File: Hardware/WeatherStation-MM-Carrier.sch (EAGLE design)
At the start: 88 parts, among them J11 microSD, J13 RJ11 - WIND, J15 MICROMOD-2222-C, J2 JTAG, J3 QWIIC_RIGHT_ANGLE, J7 RJ11 - RAIN, U1 BME280, U2 VEML6075, U3 AS3935, U5 AP7361C-33FGE

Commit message: Implementing some changes from design check list
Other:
- note added: "Range: 4.2 - 5.2V"
- moved on the sheet: C6, C7, C8, J4, L1, R19, R6, U3

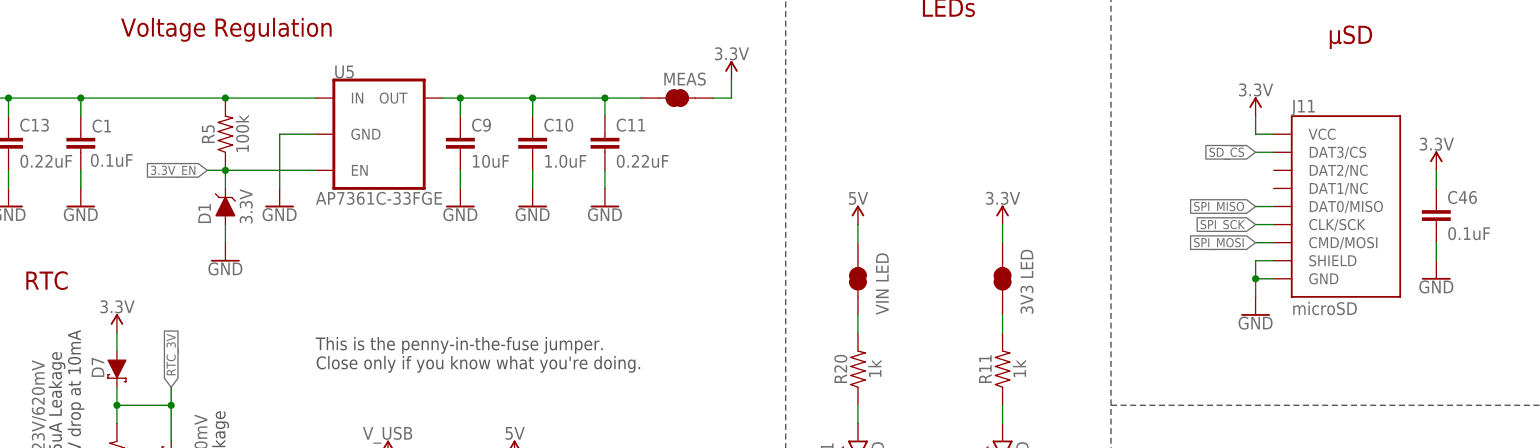
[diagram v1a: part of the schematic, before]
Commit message: Added jumper on 3.3V_EN
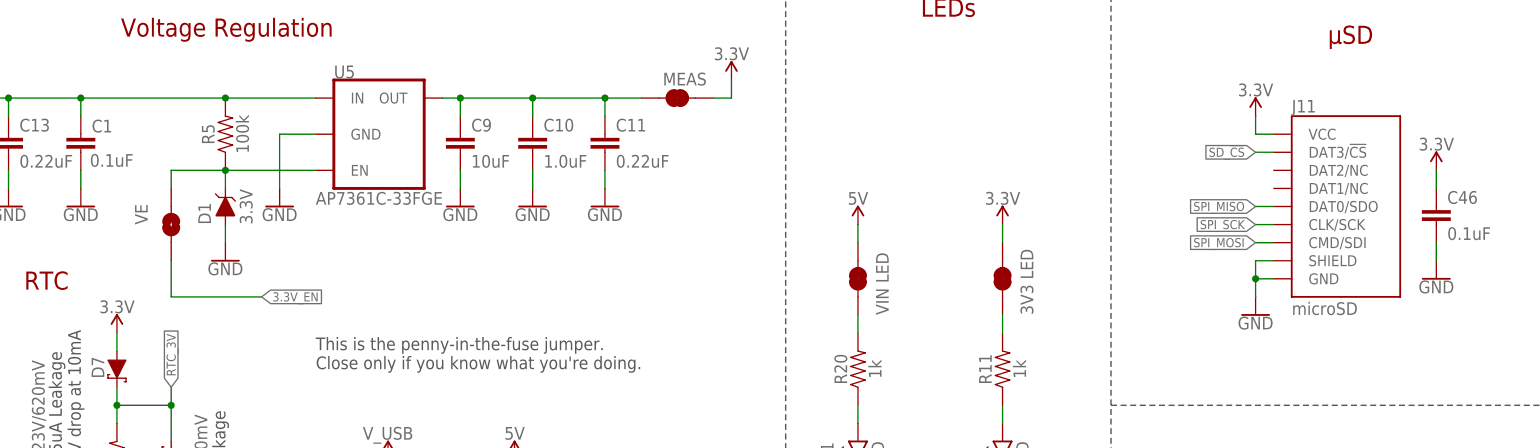
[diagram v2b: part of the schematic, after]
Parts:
- added JP6: VE, SparkFun-Jumpers:JUMPER-SMT_2_NO_SILK
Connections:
- net 3.3V_EN: now also JP6.1, JP6.2
- net SD_!CS!: now also J11.DAT3/!CS!; no longer J11.DAT3/CS
- net SPI_MISO: now also J11.DAT0/SDO; no longer J11.DAT0/MISO
- net SPI_MOSI: now also J11.CMD/SDI; no longer J11.CMD/MOSI
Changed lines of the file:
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@@
 <part name="JP3" library="SparkFun-Jumpers" deviceset="JUMPER-SMT_2_NC_TRACE" device="_SILK" package3d_urn="urn:adsk.eagle:package:39281/1" value="UV"/>
 <part name="JP5" library="SparkFun-Jumpers" deviceset="JUMPER-SMT_3_2-NC_TRACE" device="_SILK" package3d_urn="urn:adsk.eagle:package:39289/1" value="VIN/3"/>
+<part name="JP6" library="SparkFun-Jumpers" deviceset="JUMPER-SMT_2_NO" device="_SILK" package3d_urn="urn:adsk.eagle:package:39279/1" value="VE"/>
 </parts>
 <sheets>
@@
 <attribute name="VALUE" x="136.779" y="30.48" size="1.778" layer="96" font="vector" rot="R270" align="top-left"/>
 </instance>
+<instance part="JP6" gate="G$1" x="35.56" y="241.3" smashed="yes" rot="R90">
+<attribute name="VALUE" x="30.48" y="241.3" size="1.778" layer="96" font="vector" rot="R90" align="top-left"/>
+</instance>
 </instances>
 <busses>
@@
 <wire x1="190.5" y1="238.76" x2="187.96" y2="238.76" width="0.1524" layer="91"/>
 <label x="187.96" y="238.76" size="1.27" layer="95" rot="R180" xref="yes"/>
-<pinref part="J11" gate="G$1" pin="CMD/MOSI"/>
+<pinref part="J11" gate="G$1" pin="CMD/SDI"/>
 </segment>
 <segment>
@@
 <wire x1="190.5" y1="243.84" x2="187.96" y2="243.84" width="0.1524" layer="91"/>
 <label x="187.96" y="243.84" size="1.27" layer="95" rot="R180" xref="yes"/>
-<pinref part="J11" gate="G$1" pin="DAT0/MISO"/>
+<pinref part="J11" gate="G$1" pin="DAT0/SDO"/>
 </segment>
 <segment>
@@
 <wire x1="190.5" y1="251.46" x2="187.96" y2="251.46" width="0.1524" layer="91"/>
 <label x="187.96" y="251.46" size="1.27" layer="95" rot="R180" xref="yes"/>
-<pinref part="J11" gate="G$1" pin="DAT3/CS"/>
+<pinref part="J11" gate="G$1" pin="DAT3/!CS!"/>
 </segment>
 <segment>
@@
 <pinref part="U5" gate="G$1" pin="EN"/>
 <wire x1="55.88" y1="248.92" x2="43.18" y2="248.92" width="0.1524" layer="91"/>
-<label x="40.64" y="248.92" size="1.27" layer="95" rot="R180" xref="yes"/>
 <pinref part="D1" gate="G$1" pin="C"/>
-<wire x1="43.18" y1="248.92" x2="40.64" y2="248.92" width="0.1524" layer="91"/>
-<wire x1="43.18" y1="246.38" x2="43.18" y2="248.92" width="0.1524" layer="91"/>
 <junction x="43.18" y="248.92"/>
 <pinref part="R5" gate="G$1" pin="1"/>
+<pinref part="JP6" gate="G$1" pin="2"/>
+<wire x1="35.56" y1="246.38" x2="35.56" y2="248.92" width="0.1524" layer="91"/>
+<wire x1="35.56" y1="248.92" x2="43.18" y2="248.92" width="0.1524" layer="91"/>
+<wire x1="43.18" y1="248.92" x2="43.18" y2="246.38" width="0.1524" layer="91"/>
 </segment>
 <segment>
@@
 <pinref part="J15" gate="J1" pin="3.3V_EN"/>
 </segment>
-</net>
+<segment>
+<pinref part="JP6" gate="G$1" pin="1"/>
+<wire x1="35.56" y1="236.22" x2="35.56" y2="231.14" width="0.1524" layer="91"/>
+<wire x1="35.56" y1="231.14" x2="48.26" y2="231.14" width="0.1524" layer="91"/>
+<label x="48.26" y="231.14" size="1.27" layer="95" xref="yes"/>
+</segment>
+</net>

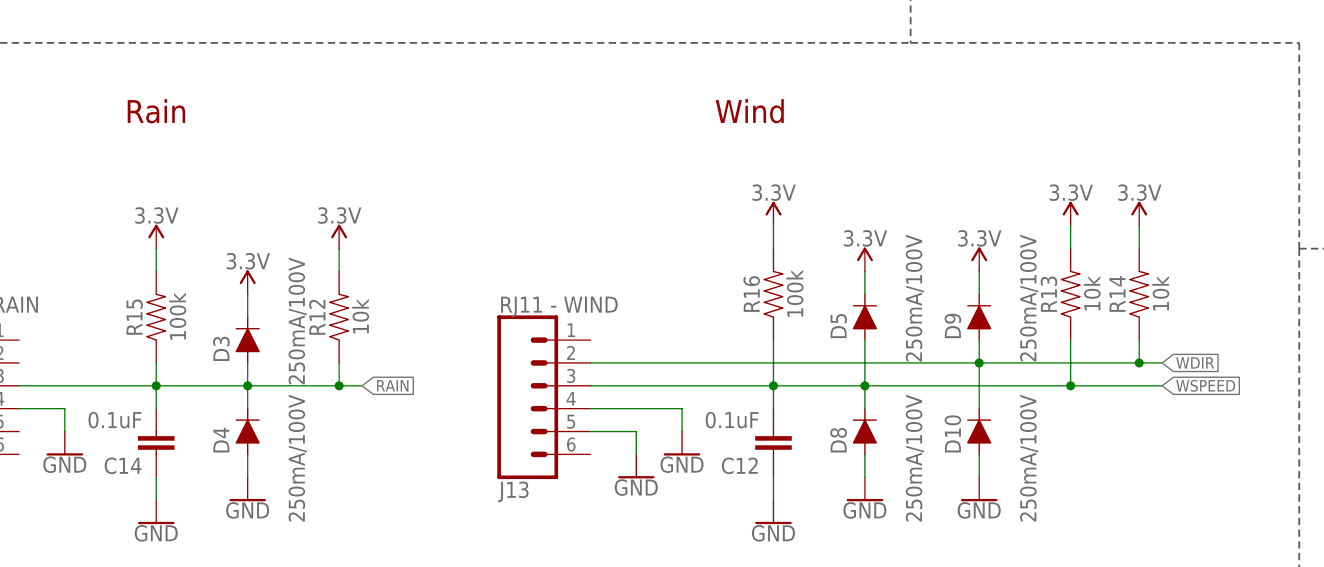
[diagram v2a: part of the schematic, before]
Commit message: Update weather meter circuitry
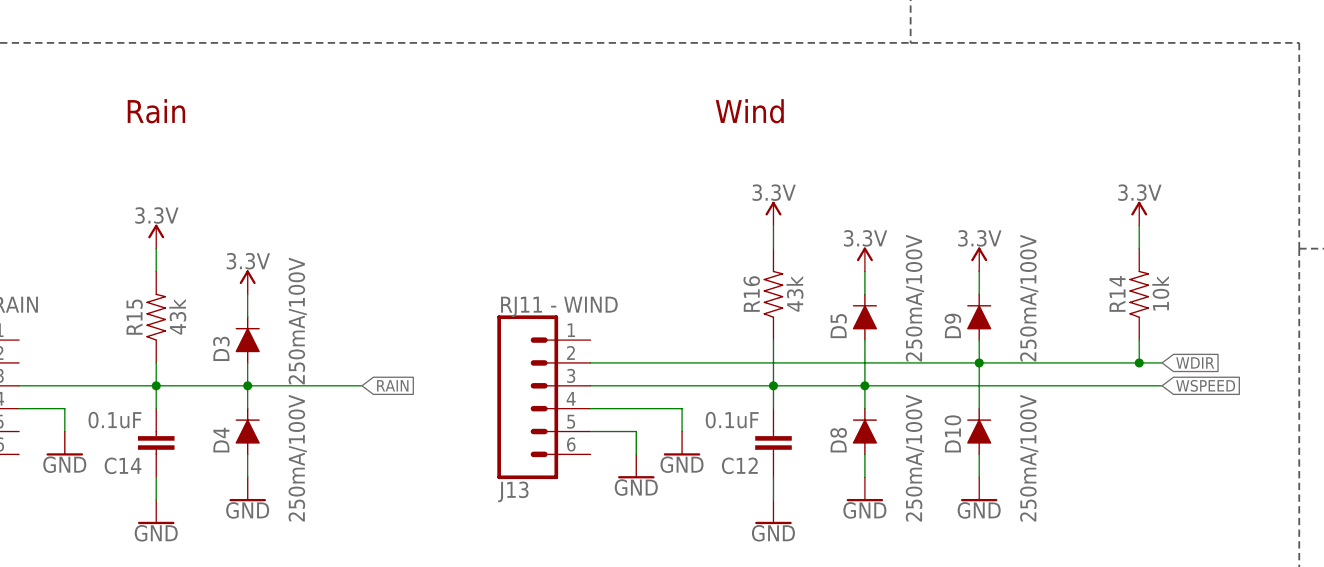
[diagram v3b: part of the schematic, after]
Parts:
- removed R12, R13: 10k, SparkFun-Resistors:10KOHM-0603-1/10W-1%
- R15, R16: value 100k -> 43k; device SparkFun-Resistors:100KOHM-0603-1/10W-1% -> SparkFun-Resistors:43KOHM-0603-1/10W-1%
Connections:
- net 3.3V: no longer R12.2, R13.2
- net RAIN: no longer R12.1
- net WSPEED: no longer R13.1
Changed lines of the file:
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@@
 <part name="GND39" library="SparkFun-PowerSymbols" deviceset="GND" device=""/>
 <part name="GND43" library="SparkFun-PowerSymbols" deviceset="GND" device=""/>
-<part name="R12" library="SparkFun-Resistors" deviceset="10KOHM" device="-0603-1/10W-1%" value="10k"/>
-<part name="SUPPLY15" library="SparkFun-PowerSymbols" deviceset="3.3V" device=""/>
-<part name="R13" library="SparkFun-Resistors" deviceset="10KOHM" device="-0603-1/10W-1%" value="10k"/>
 <part name="R14" library="SparkFun-Resistors" deviceset="10KOHM" device="-0603-1/10W-1%" value="10k"/>
-<part name="SUPPLY21" library="SparkFun-PowerSymbols" deviceset="3.3V" device=""/>
 <part name="SUPPLY22" library="SparkFun-PowerSymbols" deviceset="3.3V" device=""/>
 <part name="D3" library="SparkFun-DiscreteSemi" deviceset="DIODE" device="-BAS16J" value="250mA/100V"/>
@@
 <part name="GND33" library="SparkFun-PowerSymbols" deviceset="GND" device=""/>
 <part name="GND34" library="SparkFun-PowerSymbols" deviceset="GND" device=""/>
-<part name="R15" library="SparkFun-Resistors" deviceset="100KOHM" device="-0603-1/10W-1%" value="100k"/>
-<part name="R16" library="SparkFun-Resistors" deviceset="100KOHM" device="-0603-1/10W-1%" value="100k"/>
+<part name="R15" library="SparkFun-Resistors" deviceset="43KOHM" device="-0603-1/10W-1%" value="43k"/>
+<part name="R16" library="SparkFun-Resistors" deviceset="43KOHM" device="-0603-1/10W-1%" value="43k"/>
 <part name="C12" library="SparkFun-Capacitors" deviceset="0.1UF" device="-0603-25V-(+80/-20%)" value="0.1uF"/>
 <part name="C14" library="SparkFun-Capacitors" deviceset="0.1UF" device="-0603-25V-(+80/-20%)" value="0.1uF"/>
@@
 <attribute name="VALUE" x="96.52" y="243.586" size="1.778" layer="96" align="top-center"/>
 </instance>
-<instance part="R12" gate="G$1" x="223.52" y="142.24" smashed="yes" rot="R90">
-<attribute name="NAME" x="221.996" y="142.24" size="1.778" layer="95" font="vector" rot="R90" align="bottom-center"/>
-<attribute name="VALUE" x="225.044" y="142.24" size="1.778" layer="96" font="vector" rot="R90" align="top-center"/>
-</instance>
-<instance part="SUPPLY15" gate="G$1" x="223.52" y="149.86" smashed="yes">
-<attribute name="VALUE" x="223.52" y="152.654" size="1.778" layer="96" align="bottom-center"/>
-</instance>
-<instance part="R13" gate="G$1" x="304.8" y="144.78" smashed="yes" rot="R90">
-<attribute name="NAME" x="303.276" y="144.78" size="1.778" layer="95" font="vector" rot="R90" align="bottom-center"/>
-<attribute name="VALUE" x="306.324" y="144.78" size="1.778" layer="96" font="vector" rot="R90" align="top-center"/>
-</instance>
 <instance part="R14" gate="G$1" x="312.42" y="144.78" smashed="yes" rot="R90">
 <attribute name="NAME" x="310.896" y="144.78" size="1.778" layer="95" font="vector" rot="R90" align="bottom-center"/>
 <attribute name="VALUE" x="313.944" y="144.78" size="1.778" layer="96" font="vector" rot="R90" align="top-center"/>
-</instance>
-<instance part="SUPPLY21" gate="G$1" x="304.8" y="152.4" smashed="yes">
-<attribute name="VALUE" x="304.8" y="155.194" size="1.778" layer="96" align="bottom-center"/>
 </instance>
 <instance part="SUPPLY22" gate="G$1" x="312.42" y="152.4" smashed="yes">
@@
 <pinref part="SUPPLY11" gate="G$1" pin="3.3V"/>
 <wire x1="325.12" y1="248.92" x2="325.12" y2="246.38" width="0.1524" layer="91"/>
-</segment>
-<segment>
-<pinref part="R12" gate="G$1" pin="2"/>
-<pinref part="SUPPLY15" gate="G$1" pin="3.3V"/>
-<wire x1="223.52" y1="147.32" x2="223.52" y2="149.86" width="0.1524" layer="91"/>
-</segment>
-<segment>
-<pinref part="R13" gate="G$1" pin="2"/>
-<pinref part="SUPPLY21" gate="G$1" pin="3.3V"/>
-<wire x1="304.8" y1="149.86" x2="304.8" y2="152.4" width="0.1524" layer="91"/>
 </segment>
 <segment>
@@
 <wire x1="187.96" y1="134.62" x2="203.2" y2="134.62" width="0.1524" layer="91"/>
 <label x="226.06" y="134.62" size="1.27" layer="95" xref="yes"/>
-<pinref part="R12" gate="G$1" pin="1"/>
 <wire x1="203.2" y1="134.62" x2="213.36" y2="134.62" width="0.1524" layer="91"/>
-<wire x1="213.36" y1="134.62" x2="223.52" y2="134.62" width="0.1524" layer="91"/>
-<wire x1="223.52" y1="134.62" x2="226.06" y2="134.62" width="0.1524" layer="91"/>
-<wire x1="223.52" y1="134.62" x2="223.52" y2="137.16" width="0.1524" layer="91"/>
-<junction x="223.52" y="134.62"/>
+<wire x1="213.36" y1="134.62" x2="226.06" y2="134.62" width="0.1524" layer="91"/>
 <pinref part="D3" gate="G$1" pin="A"/>
 <wire x1="213.36" y1="134.62" x2="213.36" y2="137.16" width="0.1524" layer="91"/>
@@
 <wire x1="251.46" y1="134.62" x2="271.78" y2="134.62" width="0.1524" layer="91"/>
 <wire x1="271.78" y1="134.62" x2="281.94" y2="134.62" width="0.1524" layer="91"/>
-<wire x1="281.94" y1="134.62" x2="304.8" y2="134.62" width="0.1524" layer="91"/>
-<wire x1="304.8" y1="134.62" x2="314.96" y2="134.62" width="0.1524" layer="91"/>
+<wire x1="281.94" y1="134.62" x2="314.96" y2="134.62" width="0.1524" layer="91"/>
 <label x="314.96" y="134.62" size="1.27" layer="95" xref="yes"/>
-<pinref part="R13" gate="G$1" pin="1"/>
-<wire x1="304.8" y1="139.7" x2="304.8" y2="134.62" width="0.1524" layer="91"/>
-<junction x="304.8" y="134.62"/>
 <pinref part="D8" gate="G$1" pin="C"/>
 <wire x1="281.94" y1="134.62" x2="281.94" y2="132.08" width="0.1524" layer="91"/>

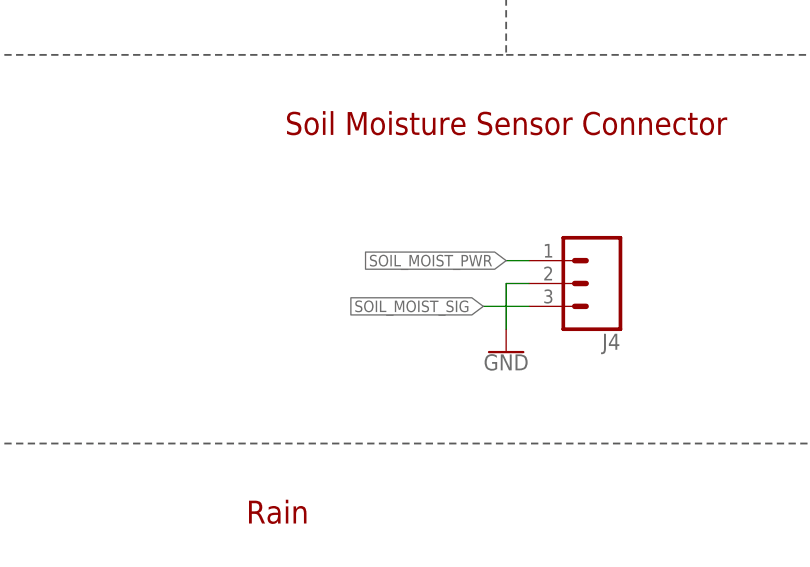
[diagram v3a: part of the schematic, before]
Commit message: Changes from Nate
Rotate soil moisture connector pins
MOSI/MISO --> COPI, POCI
Rotate LEDs
+/- silk on batt
Changed labels on jumpers
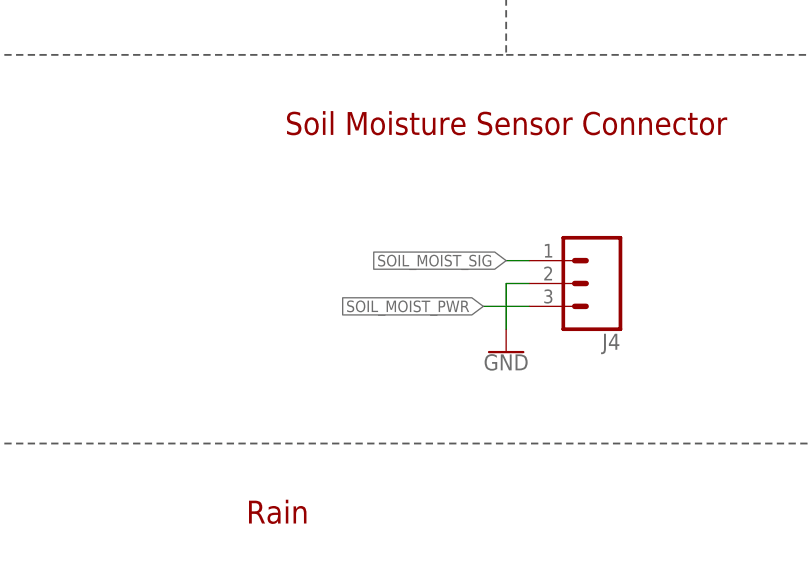
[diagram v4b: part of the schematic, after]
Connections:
- net SOIL_MOIST_PWR: now also J4.3; no longer J4.1
- net SOIL_MOIST_SIG: now also J4.1; no longer J4.3
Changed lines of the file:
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@@
 <net name="SOIL_MOIST_SIG" class="0">
-<segment>
-<wire x1="231.14" y1="187.96" x2="226.06" y2="187.96" width="0.1524" layer="91"/>
-<label x="226.06" y="187.96" size="1.27" layer="95" rot="R180" xref="yes"/>
-<pinref part="J4" gate="J$1" pin="3"/>
-</segment>
 <segment>
 <wire x1="134.62" y1="121.92" x2="137.16" y2="121.92" width="0.1524" layer="91"/>
 <label x="137.16" y="121.92" size="1.27" layer="95" xref="yes"/>
 <pinref part="J15" gate="J1" pin="A0"/>
+</segment>
+<segment>
+<pinref part="J4" gate="J$1" pin="1"/>
+<wire x1="231.14" y1="193.04" x2="228.6" y2="193.04" width="0.1524" layer="91"/>
+<label x="228.6" y="193.04" size="1.27" layer="95" rot="R180" xref="yes"/>
 </segment>
 </net>
@@
 <net name="SOIL_MOIST_PWR" class="0">
 <segment>
-<wire x1="231.14" y1="193.04" x2="228.6" y2="193.04" width="0.1524" layer="91"/>
-<pinref part="J4" gate="J$1" pin="1"/>
-<label x="228.6" y="193.04" size="1.27" layer="95" rot="R180" xref="yes"/>
-</segment>
-<segment>
 <wire x1="134.62" y1="86.36" x2="137.16" y2="86.36" width="0.1524" layer="91"/>
 <label x="137.16" y="86.36" size="1.27" layer="95" xref="yes"/>
 <pinref part="J15" gate="J1" pin="G0/BUS0"/>
 </segment>
+<segment>
+<pinref part="J4" gate="J$1" pin="3"/>
+<wire x1="231.14" y1="187.96" x2="226.06" y2="187.96" width="0.1524" layer="91"/>
+<label x="226.06" y="187.96" size="1.27" layer="95" rot="R180" xref="yes"/>
+</segment>
 </net>

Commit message: Impelemented design review changes
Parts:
- U5: value AP7361C-33FGE -> AP7361C-33FGEUDFN-8; device ublox:AP7361C-33FGE -> SparkFun-IC-Power:AP7361C-33FGEUDFN-8
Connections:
- net SPI_MISO renamed SPI_CIPO
- net SPI_MOSI renamed SPI_COPI
- new net VREG_EN: D1.C, JP6.2, R5.1, U5.EN
- net 3.3V_EN: no longer D1.C, JP6.2, R5.1, U5.EN
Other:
- note added: "Cut this jumper if you want to remove from power add an external UV sensor."
- note added: "Range: 2.2 - 6.0V"
- note added: "v10"
- note removed: "Cut this jumper if you want to not power the UV sensor."
- note removed: "v01"
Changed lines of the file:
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@@
 <part name="GND10" library="SparkFun-PowerSymbols" deviceset="GND" device=""/>
 <part name="SUPPLY5" library="SparkFun-PowerSymbols" deviceset="V_USB" device=""/>
-<part name="U5" library="ublox" deviceset="AP7361C-33FGE" device=""/>
+<part name="U5" library="SparkFun-IC-Power" deviceset="AP7361C-33FGE" device="UDFN-8"/>
 <part name="SUPPLY6" library="SparkFun-PowerSymbols" deviceset="3.3V" device=""/>
 <part name="GND20" library="SparkFun-PowerSymbols" deviceset="GND" device=""/>
@@
 <text x="391.16" y="226.06" size="1.778" layer="97" font="vector" align="center">I2C address: 0x10</text>
 <text x="386.08" y="200.66" size="1.778" layer="97" font="vector" align="center">Select SPI mode</text>
-<text x="419.1" y="7.62" size="2.54" layer="94" font="vector">v01</text>
-<text x="388.62" y="261.62" size="1.778" layer="97" font="vector">Cut this jumper if you want to
-not power the UV sensor.</text>
+<text x="419.1" y="7.62" size="2.54" layer="94" font="vector">v10</text>
+<text x="388.62" y="259.08" size="1.778" layer="97" font="vector">Cut this jumper if you want to
+remove from power add an
+external UV sensor.</text>
 <text x="284.48" y="76.2" size="1.778" layer="97" font="vector">Cut this jumper to disable
 pull-ups on I2C bus.</text>
@@
 <text x="198.12" y="266.7" size="2.54" layer="94" font="vector">μSD</text>
 <text x="27.94" y="142.24" size="1.9304" layer="97" font="vector">Range: 4.2 - 5.2V</text>
+<text x="63.5" y="266.7" size="1.778" layer="97" font="vector">Range: 2.2 - 6.0V</text>
 </plain>
 <instances>
@@
 </segment>
 </net>
-<net name="SPI_MOSI" class="0">
+<net name="SPI_COPI" class="0">
 <segment>
 <pinref part="J5" gate="G$1" pin="2"/>
@@
 </segment>
 </net>
-<net name="SPI_MISO" class="0">
+<net name="SPI_CIPO" class="0">
 <segment>
 <pinref part="J5" gate="G$1" pin="3"/>
@@
 </net>
 <net name="3.3V_EN" class="0">
-<segment>
-<pinref part="U5" gate="G$1" pin="EN"/>
-<wire x1="55.88" y1="248.92" x2="43.18" y2="248.92" width="0.1524" layer="91"/>
-<pinref part="D1" gate="G$1" pin="C"/>
-<junction x="43.18" y="248.92"/>
-<pinref part="R5" gate="G$1" pin="1"/>
-<pinref part="JP6" gate="G$1" pin="2"/>
-<wire x1="35.56" y1="246.38" x2="35.56" y2="248.92" width="0.1524" layer="91"/>
-<wire x1="35.56" y1="248.92" x2="43.18" y2="248.92" width="0.1524" layer="91"/>
-<wire x1="43.18" y1="248.92" x2="43.18" y2="246.38" width="0.1524" layer="91"/>
-</segment>
 <segment>
 <wire x1="88.9" y1="142.24" x2="86.36" y2="142.24" width="0.1524" layer="91"/>
@@
 </segment>
 </net>
+<net name="VREG_EN" class="0">
+<segment>
+<pinref part="U5" gate="G$1" pin="EN"/>
+<wire x1="55.88" y1="248.92" x2="43.18" y2="248.92" width="0.1524" layer="91"/>
+<pinref part="D1" gate="G$1" pin="C"/>
+<junction x="43.18" y="248.92"/>
+<pinref part="R5" gate="G$1" pin="1"/>
+<pinref part="JP6" gate="G$1" pin="2"/>
+<wire x1="35.56" y1="246.38" x2="35.56" y2="248.92" width="0.1524" layer="91"/>
+<wire x1="35.56" y1="248.92" x2="43.18" y2="248.92" width="0.1524" layer="91"/>
+<wire x1="43.18" y1="248.92" x2="43.18" y2="246.38" width="0.1524" layer="91"/>
+</segment>
+</net>
